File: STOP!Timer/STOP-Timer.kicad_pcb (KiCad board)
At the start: 2 copper layers, 4 parts, among them SW1 SW_Push_DPDT, U2 PEC11R-4230F-S0024, U3 PEC11R-4230F-S0024

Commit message: Update Schematic
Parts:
- removed U3: PEC11R-4230F-S0024, project_footprints:PEC11R4225FS0012
- added BZ1: Buzzer, Buzzer_Beeper:Buzzer_12x9.5RM7.6, B.Cu at (115.0, 64.2)
- added D1: LED, LED_SMD:LED_0805_2012Metric_Pad1.15x1.40mm_HandSolder, F.Cu at (73.0, 71.5)
- added D2: LED, LED_SMD:LED_0805_2012Metric_Pad1.15x1.40mm_HandSolder, F.Cu at (101.0, 71.5)
- added D3: LED, LED_SMD:LED_0805_2012Metric_Pad1.15x1.40mm_HandSolder, F.Cu at (129.0, 71.5)
- added DS1: HY1602E, Display:WC1602A, F.Cu at (67.0, 32.1)
- added J1: Foot Switch Jack, Connector_Audio:Jack_6.35mm_Neutrik_NMJ4HCD2_Horizontal, F.Cu at (111.0, 171.0)
- added J3: XLR3, Connector_Audio:Jack_XLR_Neutrik_NC3FAAH-0_Horizontal, F.Cu at (84.8, 157.7)
- added Q1: AO3401A, Package_TO_SOT_SMD:SOT-23, B.Cu at (105.0, 38.1)
- added R10: 1k, Resistor_SMD:R_0805_2012Metric_Pad1.20x1.40mm_HandSolder, F.Cu at (114.0, 117.0)
- added R11: 1k, Resistor_SMD:R_0805_2012Metric_Pad1.20x1.40mm_HandSolder, B.Cu at (141.0, 103.0)
- added R2: 1k, Resistor_SMD:R_0805_2012Metric_Pad1.20x1.40mm_HandSolder, B.Cu at (81.0, 79.0)
- added R3: 1k, Resistor_SMD:R_0805_2012Metric_Pad1.20x1.40mm_HandSolder, B.Cu at (110.0, 79.0)
- added R4: 1k, Resistor_SMD:R_0805_2012Metric_Pad1.20x1.40mm_HandSolder, B.Cu at (139.0, 79.0)
- added R5: 1k, Resistor_SMD:R_0805_2012Metric_Pad1.20x1.40mm_HandSolder, F.Cu at (114.0, 105.0)
- added R6: 1k, Resistor_SMD:R_0805_2012Metric_Pad1.20x1.40mm_HandSolder, F.Cu at (114.0, 108.0)
- added R7: 1k, Resistor_SMD:R_0805_2012Metric_Pad1.20x1.40mm_HandSolder, F.Cu at (114.0, 111.0)
- added R8: R, Resistor_SMD:R_0805_2012Metric_Pad1.20x1.40mm_HandSolder, F.Cu at (101.0, 69.0)
- added R9: 1k, Resistor_SMD:R_0805_2012Metric_Pad1.20x1.40mm_HandSolder, F.Cu at (114.0, 114.0)
- added SW2: SW_Push, Button_Switch_Keyboard:SW_Cherry_MX_1.50u_PCB, F.Cu at (101.5, 79.9)
- added SW3: SW_Push, Button_Switch_Keyboard:SW_Cherry_MX_1.50u_PCB, F.Cu at (130.5, 79.9)
- added SW4: SW_Push, Button_Switch_Keyboard:SW_Cherry_MX_1.50u_PCB, F.Cu at (101.5, 124.9)
- added SW6: SW_Push, Button_Switch_Keyboard:SW_Cherry_MX_1.50u_PCB, F.Cu at (72.5, 124.9)
- added SW7: SW_Push, Button_Switch_Keyboard:SW_Cherry_MX_1.50u_PCB, F.Cu at (130.5, 124.9)
- added U4: PCF8574, Package_SO:SSOP-20_4.4x6.5mm_P0.65mm, B.Cu at (85.0, 39.0)
- SW1: value SW_Push_DPDT -> SW_Push; footprint Button_Switch_THT:SW_Push_2P2T_Toggle_CK_PVA2xxH4xxxxxxV2 -> Button_Switch_Keyboard:SW_Cherry_MX_1.50u_PCB
- U2: value PEC11R-4230F-S0024 -> EC11E18244AU; footprint project_footprints:PEC11R4225FS0012 -> Rotary_Encoder:RotaryEncoder_Alps_EC11E-Switch_Vertical_H20mm
- moved SW1 72.1 mm to (72.5, 79.9)
- moved U2 59.3 mm to (120.5, 104.0)
- moved U1 29.9 mm to (78.2, 106.5), turned to -90 degrees
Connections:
- SW1 pad 1: unconnected-(SW1-A-Pad1) -> TIME_SEL_1
- SW1 pad 2: unconnected-(SW1-B-Pad2) -> GND
- U1 pad 18: unconnected-(U1-GND-Pad18) -> GND
- U1 pad 23: unconnected-(U1-GND-Pad23) -> GND
- U1 pad 3: unconnected-(U1-GND-Pad3) -> GND
- U1 pad 38: unconnected-(U1-GND-Pad38) -> GND
- U1 pad 40: unconnected-(U1-VBUS-Pad40) -> VCC
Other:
- board outline added: 93 x 162 mm

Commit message: Update 31 03 2026
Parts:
- added ?: , , F.Cu at (158.0, 25.0)
- added ?: , , F.Cu at (248.0, 25.0)
- added ?: , , F.Cu at (248.0, 145.0)
- added ?: , , F.Cu at (158.0, 145.0)
- added H1: MountingHole_Pad, MountingHole:MountingHole_3.2mm_M3_DIN965_Pad, F.Cu at (55.0, 25.0)
- added H2: MountingHole_Pad, MountingHole:MountingHole_3.2mm_M3_DIN965_Pad, F.Cu at (145.0, 25.0)
- added H3: MountingHole_Pad, MountingHole:MountingHole_3.2mm_M3_DIN965_Pad, F.Cu at (55.0, 145.0)
- added H4: MountingHole_Pad, MountingHole:MountingHole_3.2mm_M3_DIN965_Pad, F.Cu at (145.0, 145.0)
- added J2: Conn_01x04_Pin, Connector_PinHeader_2.54mm:PinHeader_1x04_P2.54mm_Vertical, F.Cu at (55.0, 44.0)
- added J4: Conn_01x04_Pin, Connector_PinHeader_2.54mm:PinHeader_1x04_P2.54mm_Vertical, F.Cu at (158.0, 44.0)
- added JP1: SolderJumper_2_Bridged, Jumper:SolderJumper-2_P1.3mm_Bridged_Pad1.0x1.5mm, B.Cu at (82.0, 44.6)
- added Q2: AO3401A, Package_TO_SOT_SMD:SOT-23, B.Cu at (107.0, 124.1)
- added R1: 4.7k, Resistor_SMD:R_0805_2012Metric_Pad1.20x1.40mm_HandSolder, B.Cu at (109.0, 35.0)
- added RV1: 20k, Potentiometer_THT:Potentiometer_Bourns_3386W_Horizontal, B.Cu at (70.5, 40.0)
- added SW8: SW_SPDT, Button_Switch_SMD:SW_SPDT_PCM12, F.Cu at (114.5, 22.1)
- added mouse-bite-3mm-slot: VAL**, Panelization:mouse-bite-3mm-slot, F.Cu at (151.5, 28.0)
- added mouse-bite-3mm-slot: VAL**, Panelization:mouse-bite-3mm-slot, F.Cu at (151.5, 142.0)
- added mouse-bite-3mm-slot: VAL**, Panelization:mouse-bite-3mm-slot, F.Cu at (151.5, 87.0)
- J1: footprint Connector_Audio:Jack_6.35mm_Neutrik_NMJ4HCD2_Horizontal -> Connector_Audio:Jack_6.35mm_Neutrik_NMJ4HFD2_Horizontal; moved to B.Cu
- J3: footprint Connector_Audio:Jack_XLR_Neutrik_NC3FAAH-0_Horizontal -> Connector_Audio:Jack_XLR_Neutrik_NC3MAAH-0_Horizontal; moved to B.Cu
- R10: value 1k -> 4.7k; moved to B.Cu
- R5, R6, R7, R9: moved to B.Cu
- SW1, SW2, SW3, SW4, SW6, SW7: footprint Button_Switch_Keyboard:SW_Cherry_MX_1.50u_PCB -> project_footprints:SW_Cherry_MX_1.50u_PCB_3dmodel
- U2: footprint Rotary_Encoder:RotaryEncoder_Alps_EC11E-Switch_Vertical_H20mm -> project_footprints:EC11E18244AU
- moved R6 113.3 mm to (154.0, 2.00), turned to -90 degrees
- moved R8 103.0 mm to (204.0, 72.0), turned to 90 degrees
- moved D3 102.0 mm to (231.0, 72.0), turned to 90 degrees
- moved D2 101.0 mm to (202.0, 72.0), turned to 90 degrees
- moved D1 100.0 mm to (173.0, 72.0), turned to 90 degrees
- moved U1 76.4 mm to (130.2, 50.6), turned to 90 degrees
- moved R10 74.0 mm to (93.0, 46.0), turned to -90 degrees
- moved R9 48.7 mm to (130.0, 68.0), turned to -90 degrees
- moved R7 44.9 mm to (127.0, 68.0), turned to -90 degrees
- moved SW7 44.0 mm to (86.5, 124.9)
- moved R2 41.5 mm to (121.0, 68.0)
- moved J1 40.0 mm to (129.0, 135.2), turned to 0 degrees
- moved J3 39.5 mm to (112.0, 129.1), turned to 180 degrees
- moved R5 38.3 mm to (124.0, 68.0), turned to -90 degrees
- moved R11 35.7 mm to (134.0, 68.0)
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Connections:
- D1 pad 2: INDICATOR_TIME_1 -> Net-(D1-A)
- D2 pad 2: INDICATOR_TIME_2 -> Net-(D2-A)
- D3 pad 2: INDICATOR_TIME_3 -> Net-(D3-A)
- DS1 pad 3: VCC -> LCD_CONTRAST
- J1 pad S: FOOT_ENABLE -> START_SEL
- J3 pad 3: CTRL_POWER_ENABLE -> Net-(Q2-S)
- R10 pad 1: VCC -> I2C_SDA
- R10 pad 2: START_SEL -> GND
- R5 pad 2: FOOT_ENABLE -> START_SEL
- R8 pad 2: GND -> Net-(J4-Pin_4)
- U1 pad 10: unconnected-(U1-GP7/SPI0_TX/_I2C1_SCL-Pad10) -> START_SEL
- U1 pad 11: unconnected-(U1-GP8/SPI1_RX/I2C0_SDA/UART1_TX-Pad11) -> TIME_SEL_1
- U1 pad 12: unconnected-(U1-GP9/SPI1_CSn/I2C0_SCL/UART1_RX-Pad12) -> TIME_SEL_2
- U1 pad 13: unconnected-(U1-GND-Pad13) -> TIME_SEL_3
- U1 pad 16: unconnected-(U1-GP12/SPI1_RX/I2C0_SDA/UART0_TX-Pad16) -> CTRL_POWER_ENABLE
- U1 pad 17: unconnected-(U1-GP13/SPI1_CSn/I2C0_SCL/UART0_RX-Pad17) -> INDICATOR_TIME_3
- U1 pad 19: unconnected-(U1-GP14/SPI1_SCK/I2C1_SCL-Pad19) -> INDICATOR_TIME_2
- U1 pad 20: unconnected-(U1-GP15/SPI1_TX/I2C1_SCL-Pad20) -> INDICATOR_TIME_1
- U1 pad 26: unconnected-(U1-GP20/I2C0_SDA-Pad26) -> I2C_SDA
- U1 pad 27: unconnected-(U1-GP21/I2C0_SCL-Pad27) -> I2C_SCL
- U1 pad 32: unconnected-(U1-GP27/ADC1/I2C1_SCL-Pad32) -> LCD_BACKLIGHT_ENABLE
- U1 pad 33: unconnected-(U1-GND/AGND-Pad33) -> GND
- U1 pad 39: unconnected-(U1-VSYS-Pad39) -> BUZZ_SIGNAL
- U1 pad 4: unconnected-(U1-GP2/SPIO_SCK/I2C1_SDA-Pad4) -> ENCODER_A
- U1 pad 5: unconnected-(U1-GP3/SPIO_TX/I2C1SCL-Pad5) -> ENCODER_B
- U1 pad 7: unconnected-(U1-GP5/SPIO_CSn/I2C0_SCL-Pad7) -> VIEW_SEL
- U1 pad 8: unconnected-(U1-GND-Pad8) -> GND
- U1 pad 9: unconnected-(U1-GP6/SPIO_SCK/I2C1_SDA-Pad9) -> MODE_SEL
- U4 pad 7: LCD_BT -> Net-(JP1-B)
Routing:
- net VCC: track 0.00 -> 360.7 mm, vias 0 -> 12
- net START_SEL: track 0.00 -> 160.8 mm
- net Net-(D3-A): track 0.00 -> 101.3 mm
- net VIEW_SEL: track 0.00 -> 90.5 mm, vias 0 -> 2
- net Net-(J4-Pin_4): track 0.00 -> 79.8 mm, vias 0 -> 1
- net CTRL_POWER_ENABLE: track 0.00 -> 73.6 mm, vias 0 -> 2
- net Net-(D2-A): track 0.00 -> 70.5 mm
- net TIME_SEL_1: track 0.00 -> 68.2 mm
- net INDICATOR_TIME_3: track 0.00 -> 62.1 mm
- net MODE_SEL: track 0.00 -> 59.5 mm
- net Net-(D1-K): track 0.00 -> 58.0 mm
- net LCD_BACKLIGHT_ENABLE: track 0.00 -> 57.3 mm, vias 0 -> 2
- net INDICATOR_TIME_2: track 0.00 -> 56.0 mm
- net ENCODER_SEL: track 0.00 -> 53.8 mm
- net INDICATOR_TIME_1: track 0.00 -> 51.6 mm
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- added copper zone on B.Cu, net GND
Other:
- board size 93 x 162 mm -> 203 x 130 mm
- board text added: "BUZZ OFF ON"
- board text added: "MENU"
- board text added: "MODE"
- board text added: "START"
- board text added: "TIME 1"
- board text added: "TIME 2"
- board text added: "TIME 3"
- board text added: "VIEW"

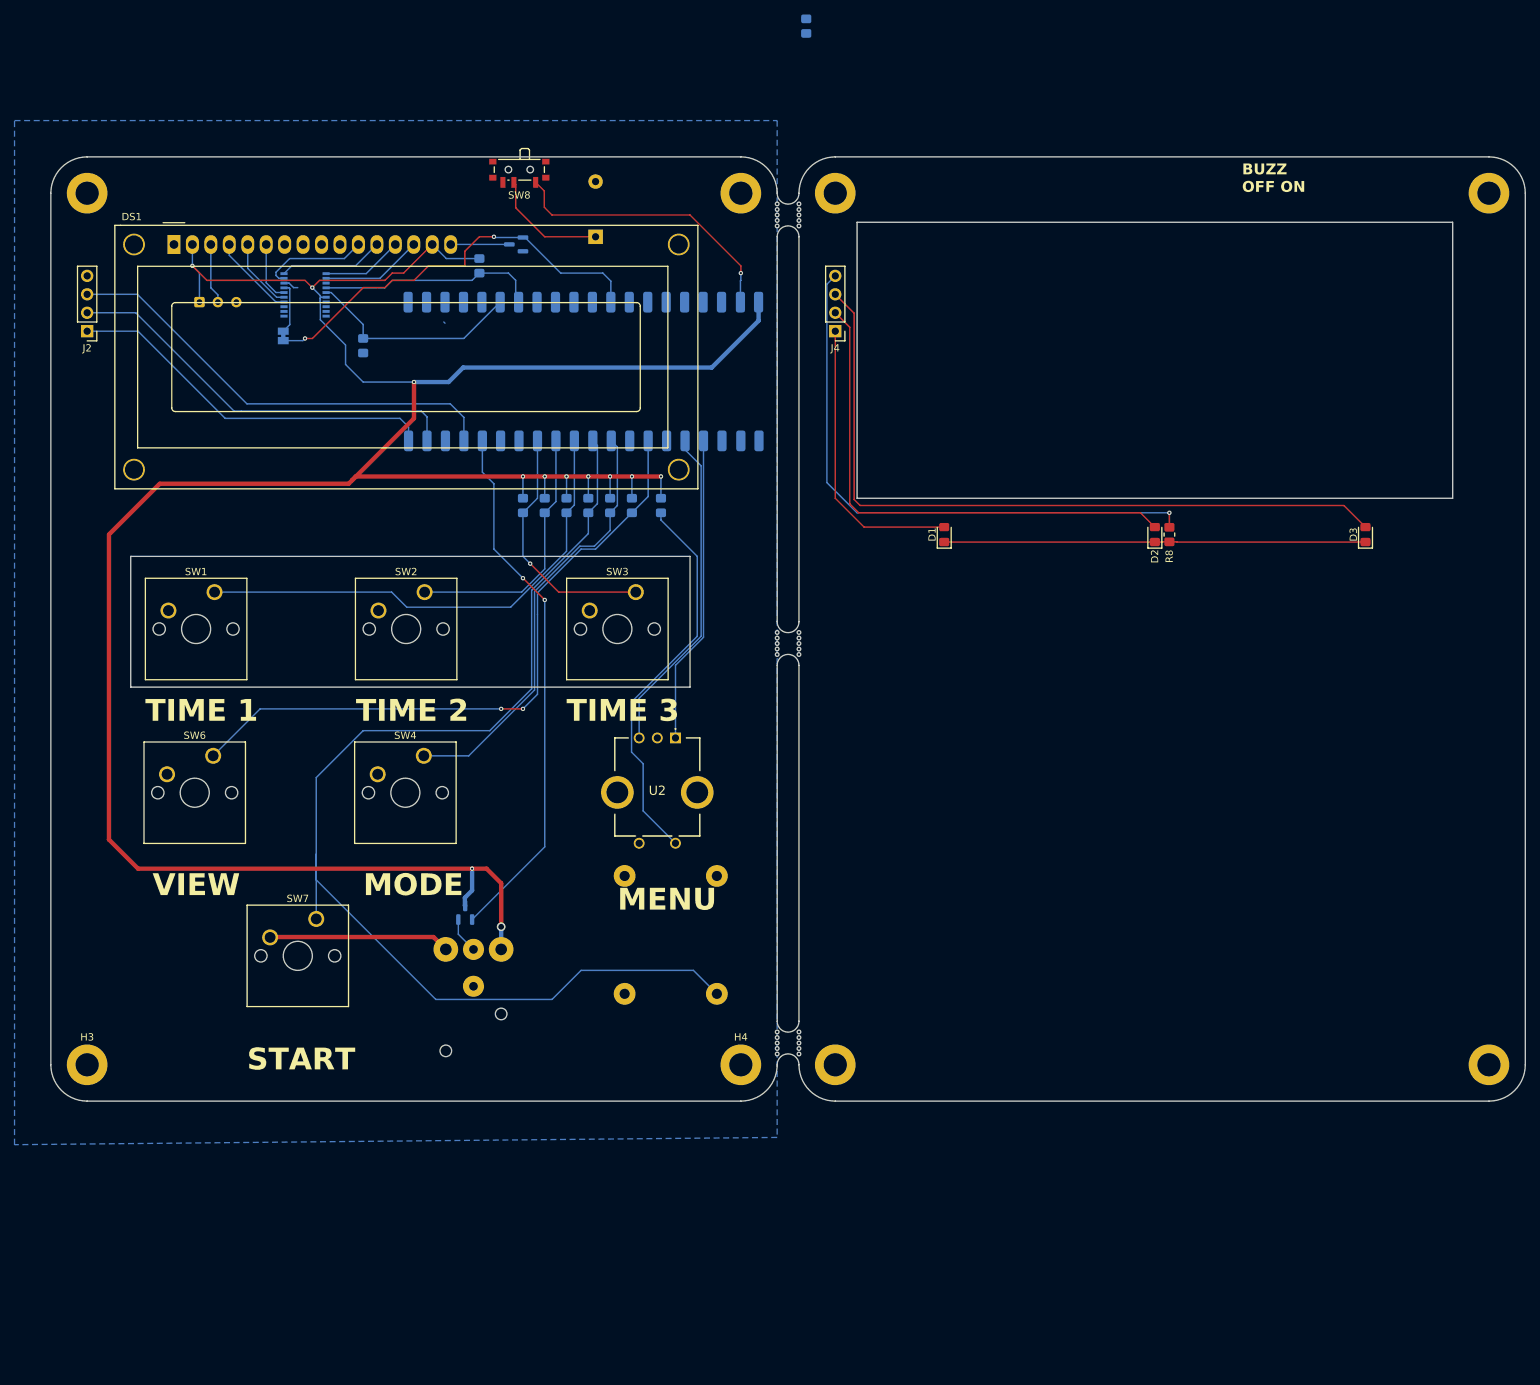
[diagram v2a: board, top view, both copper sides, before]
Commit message: Change Look of Board
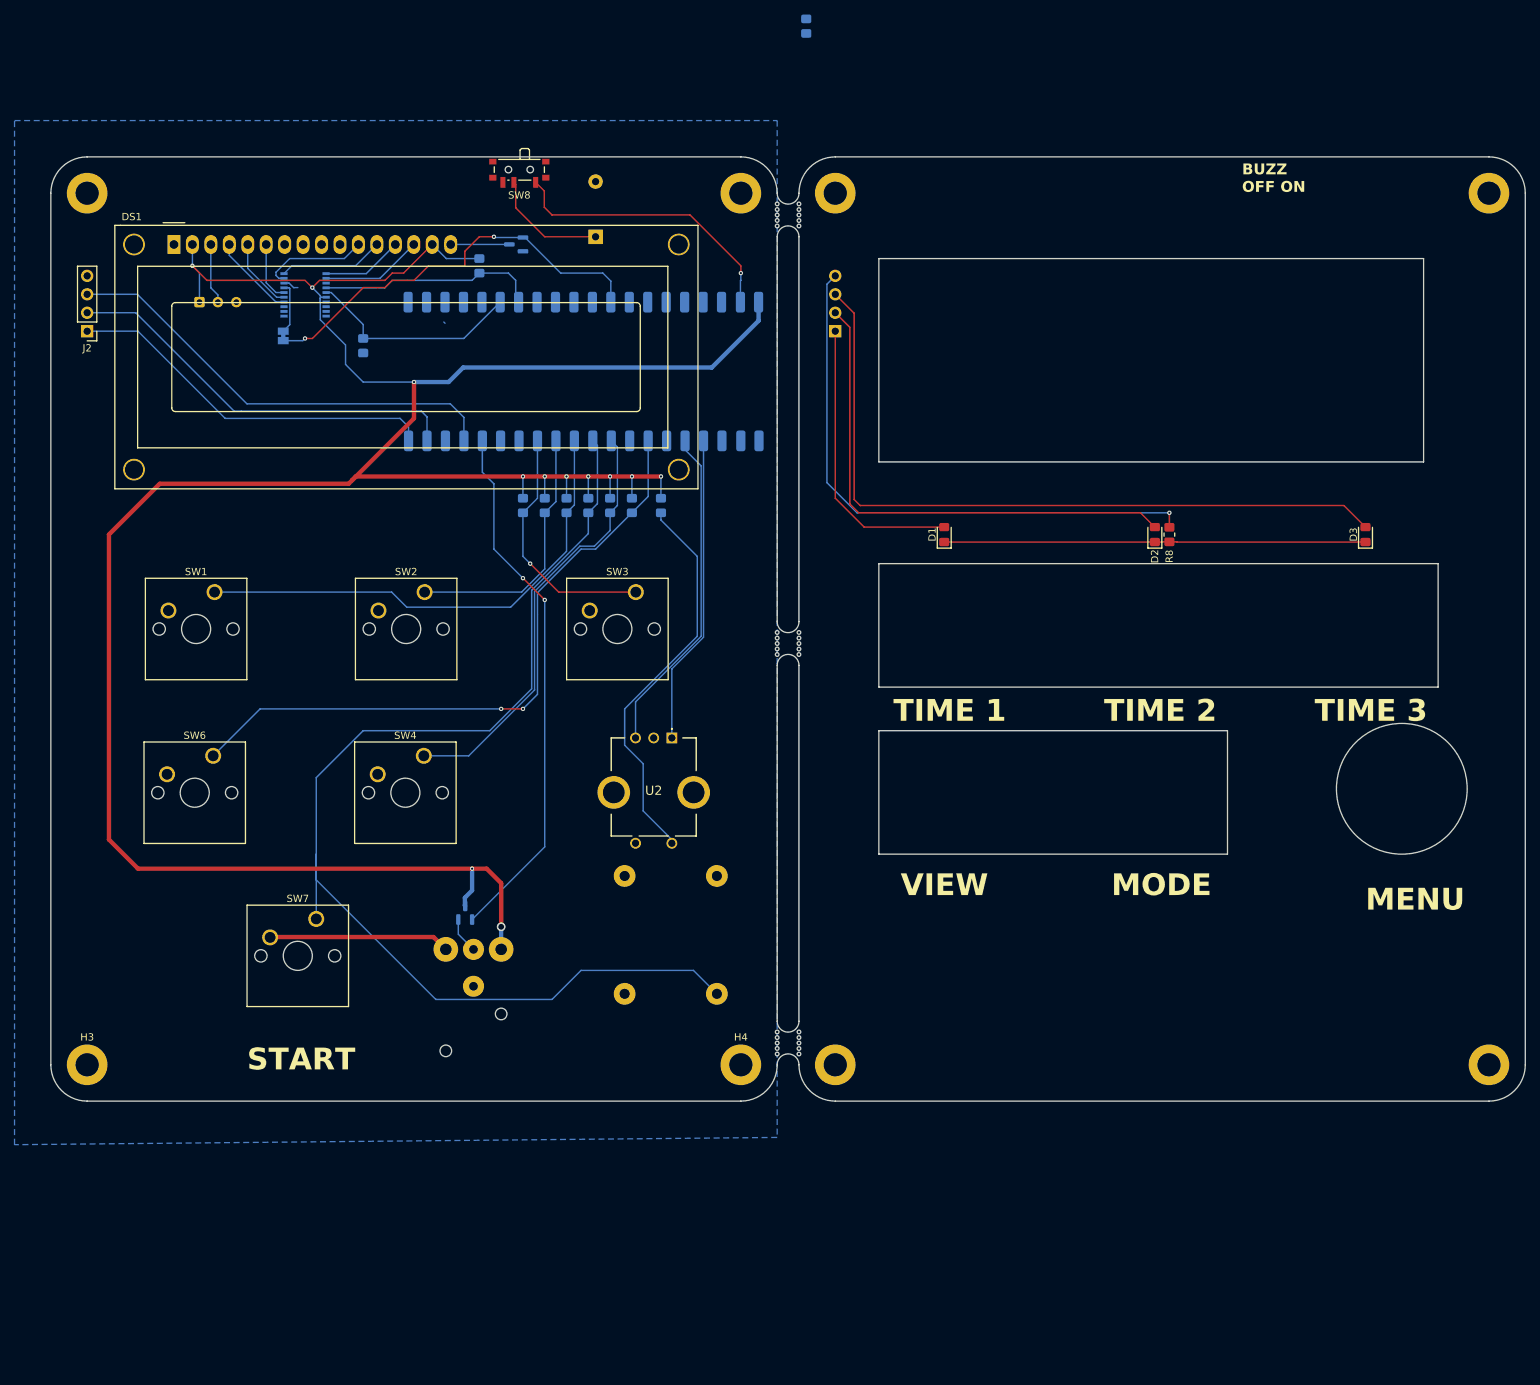
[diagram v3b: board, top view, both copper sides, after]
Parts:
- J4: footprint Connector_PinHeader_2.54mm:PinHeader_1x04_P2.54mm_Vertical -> Connector_PinSocket_2.54mm:PinSocket_1x04_P2.54mm_Vertical; moved to B.Cu
- moved U2 0.50 mm to (135.5, 100.0)
- turned J4 to 0 degrees
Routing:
- net ENCODER_SEL: track 53.8 -> 54.6 mm
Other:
- outline, holes or cut-outs redrawn

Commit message: update to order version 1.0
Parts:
- removed R11, R2, R3, R4, R5, R7, R9: 1k, Resistor_SMD:R_0805_2012Metric_Pad1.20x1.40mm_HandSolder
- J1: footprint Connector_Audio:Jack_6.35mm_Neutrik_NMJ4HFD2_Horizontal -> project_footprints:NEUTRIK NMJ2HF-S
- RV1: footprint Potentiometer_THT:Potentiometer_Bourns_3386W_Horizontal -> Potentiometer_THT:Potentiometer_Bourns_3386P_Vertical
- SW8: moved to B.Cu
- moved R6 33.6 mm to (147.5, 35.0), turned to 90 degrees
- moved SW7 14.3 mm to (72.3, 127.0)
- moved J3 13.1 mm to (102.8, 138.4)
- moved U2 12.5 mm to (135.0, 112.5)
- moved Q2 10.8 mm to (100.5, 132.6)
- moved J1 9.97 mm to (127.0, 145.0), turned to 180 degrees
- moved R8 3.14 mm to (205.0, 69.0)
- moved D1 2.97 mm to (173.0, 69.0)
- moved D2 2.97 mm to (202.0, 69.0)
- moved D3 2.97 mm to (231.0, 69.0)
- moved ? 2.83 mm to (160.0, 27.0)
- moved ? 2.83 mm to (246.0, 27.0)
- moved ? 2.83 mm to (246.0, 143.0)
- moved ? 2.83 mm to (160.0, 143.0)
- moved H1 2.83 mm to (57.0, 27.0)
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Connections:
- U1 pad 34: unconnected-(U1-GP28/ADC2-Pad34) -> BUZZ_SIGNAL
- U1 pad 39: BUZZ_SIGNAL -> VCC
- U1 pad 40: VCC -> unconnected-(U1-VBUS-Pad40)
- U1 pad 6: unconnected-(U1-GP4/SPIO_RX/I2C0_SDA/_UART1_TX-Pad6) -> ENCODER_SEL
- U2 pad C1: unconnected-(U2-PadC1) -> GND
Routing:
- net VCC: track 360.7 -> 241.9 mm, vias 12 -> 3
- net ENCODER_SEL: track 54.6 -> 76.9 mm
- net GND: track 27.3 -> 7.91 mm, vias 0 -> 1
- net START_SEL: track 160.8 -> 175.8 mm
- net CTRL_POWER_ENABLE: track 73.6 -> 87.8 mm
- net ENCODER_A: track 42.9 -> 55.4 mm
- net ENCODER_B: track 45.8 -> 57.8 mm
- net BUZZ_SIGNAL: track 39.3 -> 29.5 mm, vias 1 -> 0
- net Net-(J4-Pin_4): track 79.8 -> 74.4 mm
- net Net-(BZ1-+): track 16.3 -> 13.5 mm
- net Net-(D3-A): track 101.3 -> 98.9 mm
- net Net-(D2-A): track 70.5 -> 68.2 mm
- net MODE_SEL: track 59.5 -> 57.7 mm
- net LCD_CONTRAST: track 8.34 -> 6.75 mm
- net Net-(D1-A): track 39.6 -> 38.4 mm
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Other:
- board size 203 x 130 mm -> 203 x 140 mm
- board text added: "+"
- board text added: "BUZZ ON OFF"
- board text added: "CONTROL BOX"
- board text added: "FOOT SWITCH"
- board text added: "JLCJLCJLCJLC"
- board text added: "STOP"
- board text added: "STOP! TIMER V 1.0 04/26 P.P."
- board text added: "TIMER"
- board text added: "V 1.0 04/26"
- board text removed: "BUZZ OFF ON"
- board text removed: "MENU"

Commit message: Update
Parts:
- RV1: footprint Potentiometer_THT:Potentiometer_Bourns_3386P_Vertical -> Potentiometer_THT:Potentiometer_Bourns_3386W_Horizontal
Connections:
- U1 pad 21: unconnected-(U1-GP16/SPI0_RX/I2C0_SDA/UART0_TX-Pad21) -> LCD_RS
- U1 pad 22: unconnected-(U1-GP17/SPI0_CSn/I2C0_SCL/UART0_RX-Pad22) -> LCD_E
- U1 pad 24: unconnected-(U1-GP18/SPI0_SCK/I2C1_SDA-Pad24) -> LCD_DB4
- U1 pad 25: unconnected-(U1-GP19/SPI0_TX/I2C1_SCL-Pad25) -> LCD_DB5
- U1 pad 29: unconnected-(U1-GP22-Pad29) -> LCD_DB6
- U1 pad 31: unconnected-(U1-GP26/ADC0/I2C1_SDA-Pad31) -> LCD_DB7
